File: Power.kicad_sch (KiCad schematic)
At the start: 53 parts, among them J16 19V 5A DC, Q2 AON7403, Q3 AON7403, Q4 AON7403, SW1 SW_Push, U11 LM3489QMM/NOPB, U6 LM3489QMM/NOPB, U8 LM3489QMM/NOPB

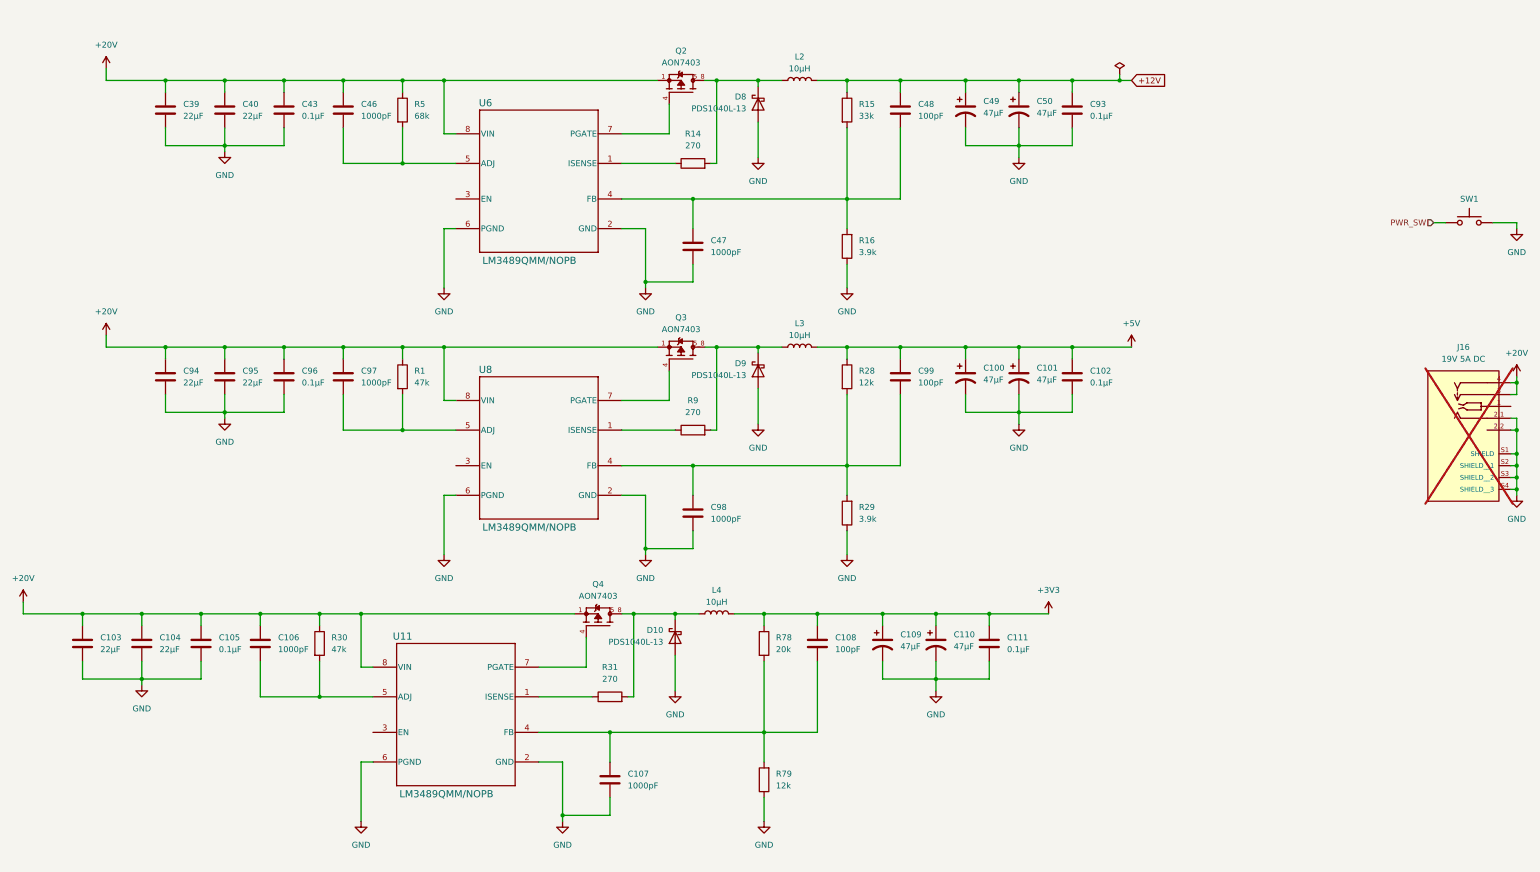
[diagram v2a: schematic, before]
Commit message: Rewired PCIe without redriver
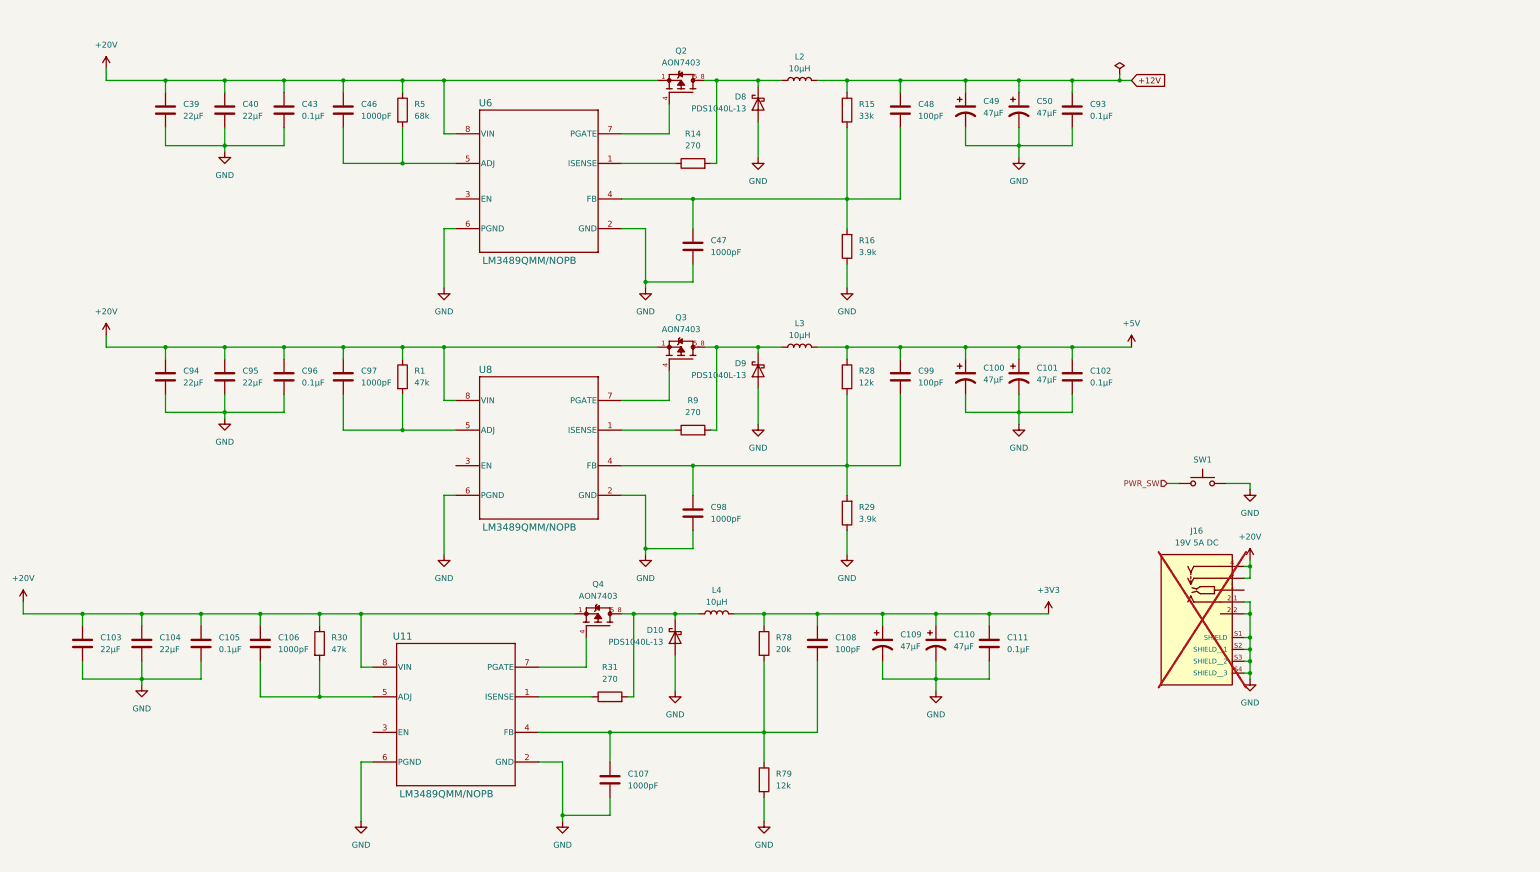
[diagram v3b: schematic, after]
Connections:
- net GND: now also R79.2; no longer R79.1
- net at C107.1, C108.2, R78.2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: now also R79.1; no longer R79.2
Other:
- moved on the sheet: J16, R79, SW1
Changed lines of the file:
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@@
 	)
 	(junction
-		(at 335.28 102.87)
+		(at 278.13 142.24)
 		(diameter 0)
 		(color 0 0 0 0)
 	)
 	(junction
-		(at 335.28 107.95)
+		(at 278.13 147.32)
 		(diameter 0)
 		(color 0 0 0 0)
@@
 	)
 	(junction
-		(at 335.28 115.57)
+		(at 278.13 154.94)
 		(diameter 0)
 		(color 0 0 0 0)
@@
 	)
 	(junction
-		(at 335.28 110.49)
+		(at 278.13 149.86)
 		(diameter 0)
 		(color 0 0 0 0)
@@
 	)
 	(junction
-		(at 335.28 113.03)
+		(at 278.13 152.4)
 		(diameter 0)
 		(color 0 0 0 0)
@@
 	)
 	(junction
-		(at 335.28 92.71)
+		(at 278.13 132.08)
 		(diameter 0)
 		(color 0 0 0 0)
@@
 	(wire
 		(pts
-			(xy 335.28 107.95) (xy 335.28 110.49)
+			(xy 278.13 147.32) (xy 278.13 149.86)
 		)
 		(stroke
@@
 	(wire
 		(pts
-			(xy 334.01 113.03) (xy 335.28 113.03)
+			(xy 276.86 152.4) (xy 278.13 152.4)
 		)
 		(stroke
@@
 	(wire
 		(pts
-			(xy 335.28 100.33) (xy 335.28 102.87)
+			(xy 278.13 139.7) (xy 278.13 142.24)
 		)
 		(stroke
@@
 	(wire
 		(pts
-			(xy 335.28 91.44) (xy 335.28 92.71)
+			(xy 278.13 130.81) (xy 278.13 132.08)
 		)
 		(stroke
@@
 	(wire
 		(pts
-			(xy 335.28 113.03) (xy 335.28 115.57)
+			(xy 278.13 152.4) (xy 278.13 154.94)
 		)
 		(stroke
@@
 	(wire
 		(pts
-			(xy 334.01 102.87) (xy 335.28 102.87)
+			(xy 276.86 142.24) (xy 278.13 142.24)
 		)
 		(stroke
@@
 	(wire
 		(pts
-			(xy 334.01 115.57) (xy 335.28 115.57)
+			(xy 276.86 154.94) (xy 278.13 154.94)
 		)
 		(stroke
@@
 	(wire
 		(pts
-			(xy 330.2 58.42) (xy 335.28 58.42)
+			(xy 273.05 114.3) (xy 278.13 114.3)
 		)
 		(stroke
@@
 	(wire
 		(pts
-			(xy 334.01 92.71) (xy 335.28 92.71)
+			(xy 276.86 132.08) (xy 278.13 132.08)
 		)
 		(stroke
@@
 	(wire
 		(pts
-			(xy 334.01 95.25) (xy 335.28 95.25)
+			(xy 276.86 134.62) (xy 278.13 134.62)
 		)
 		(stroke
@@
 	(wire
 		(pts
-			(xy 334.01 107.95) (xy 335.28 107.95)
+			(xy 276.86 147.32) (xy 278.13 147.32)
 		)
 		(stroke
@@
 	(wire
 		(pts
-			(xy 335.28 95.25) (xy 335.28 92.71)
+			(xy 278.13 134.62) (xy 278.13 132.08)
 		)
 		(stroke
@@
 	(wire
 		(pts
-			(xy 335.28 102.87) (xy 335.28 107.95)
+			(xy 278.13 142.24) (xy 278.13 147.32)
 		)
 		(stroke
@@
 	(wire
 		(pts
-			(xy 334.01 100.33) (xy 335.28 100.33)
+			(xy 276.86 139.7) (xy 278.13 139.7)
 		)
 		(stroke
@@
 	(wire
 		(pts
-			(xy 335.28 58.42) (xy 335.28 59.69)
+			(xy 278.13 114.3) (xy 278.13 115.57)
 		)
 		(stroke
@@
 	(wire
 		(pts
-			(xy 334.01 110.49) (xy 335.28 110.49)
+			(xy 276.86 149.86) (xy 278.13 149.86)
 		)
 		(stroke
@@
 	(wire
 		(pts
-			(xy 317.5 58.42) (xy 320.04 58.42)
+			(xy 260.35 114.3) (xy 262.89 114.3)
 		)
 		(stroke
@@
 	(wire
 		(pts
-			(xy 335.28 110.49) (xy 335.28 113.03)
+			(xy 278.13 149.86) (xy 278.13 152.4)
 		)
 		(stroke
@@
 	(wire
 		(pts
-			(xy 335.28 115.57) (xy 335.28 116.84)
+			(xy 278.13 154.94) (xy 278.13 156.21)
 		)
 		(stroke
@@
 	(hierarchical_label "PWR_SW"
 		(shape input)
-		(at 317.5 58.42 180)
+		(at 260.35 114.3 180)
 		(fields_autoplaced yes)
 		(effects
@@
 	(symbol
 		(lib_id "Switch:SW_Push")
-		(at 325.12 58.42 0)
+		(at 267.97 114.3 0)
 		(unit 1)
 		(exclude_from_sim no)
@@
 		(dnp no)
 		(property "Reference" "SW1"
-			(at 325.12 53.34 0)
+			(at 267.97 109.22 0)
 			(effects
 				(font
@@
 		)
 		(property "Value" "SW_Push"
-			(at 325.12 53.34 0)
+			(at 267.97 109.22 0)
 			(effects
 				(font
@@
 		)
 		(property "Footprint" "Button_Switch_SMD:SW_SPST_SKQG_WithStem"
-			(at 325.12 53.34 0)
+			(at 267.97 109.22 0)
 			(effects
 				(font
@@
 		)
 		(property "Datasheet" "~"
-			(at 325.12 53.34 0)
+			(at 267.97 109.22 0)
 			(effects
 				(font
@@
 		)
 		(property "Description" "Push button switch, generic, two pins"
-			(at 325.12 58.42 0)
+			(at 267.97 114.3 0)
 			(effects
 				(font
@@
 		)
 		(property "Part_Number" "TS-1187A-B-A-B"
-			(at 325.12 58.42 0)
+			(at 267.97 114.3 0)
 			(effects
 				(font
@@
 		)
 		(property "LCSC" "C318884"
-			(at 325.12 58.42 0)
+			(at 267.97 114.3 0)
 			(effects
 				(font
@@
 	(symbol
 		(lib_id "Device:R")
-		(at 173.99 177.8 180)
+		(at 173.99 177.8 0)
 		(unit 1)
 		(exclude_from_sim no)
@@
 					(size 1.27 1.27)
 				)
-				(justify right)
+				(justify left)
 			)
 		)
@@
 					(size 1.27 1.27)
 				)
-				(justify right)
+				(justify left)
 			)
 		)
 		(property "Footprint" "Resistor_SMD:R_0402_1005Metric"
-			(at 175.768 177.8 90)
+			(at 172.212 177.8 90)
 			(effects
 				(font
@@
 	(symbol
 		(lib_id "PJ-096H:PJ-096H")
-		(at 323.85 97.79 0)
+		(at 266.7 137.16 0)
 		(unit 1)
 		(exclude_from_sim no)
@@
 		(fields_autoplaced yes)
 		(property "Reference" "J16"
-			(at 323.85 85.09 0)
+			(at 266.7 124.46 0)
 			(effects
 				(font
@@
 		)
 		(property "Value" "19V 5A DC"
-			(at 323.85 87.63 0)
+			(at 266.7 127 0)
 			(effects
 				(font
@@
 		)
 		(property "Footprint" "PJ-096H:CUI_PJ-096H"
-			(at 323.85 97.79 0)
+			(at 266.7 137.16 0)
 			(effects
 				(font
@@
 		)
 		(property "Datasheet" "~"
-			(at 323.85 97.79 0)
+			(at 266.7 137.16 0)
 			(effects
 				(font
@@
 		)
 		(property "Description" "DC Barrel Jack"
-			(at 323.85 97.79 0)
+			(at 266.7 137.16 0)
 			(effects
 				(font
@@
 		)
 		(property "Part_Number" "PJ-096H"
-			(at 323.85 97.79 0)
+			(at 266.7 137.16 0)
 			(effects
 				(font
@@
 		)
 		(property "PARTREV" "1.0"
-			(at 323.85 97.79 0)
+			(at 266.7 137.16 0)
 			(effects
 				(font
@@
 		)
 		(property "STANDARD" "Manufacturer Recommendations"
-			(at 323.85 97.79 0)
+			(at 266.7 137.16 0)
 			(effects
 				(font
@@
 		)
 		(property "MANUFACTURER" "CUI"
-			(at 323.85 97.79 0)
+			(at 266.7 137.16 0)
 			(effects
 				(font
@@
 	(symbol
 		(lib_id "XG_Mobile:+20V")
-		(at 335.28 91.44 0)
+		(at 278.13 130.81 0)
 		(unit 1)
 		(exclude_from_sim no)
@@
 		(fields_autoplaced yes)
 		(property "Reference" "#PWR0105"
-			(at 335.28 95.25 0)
+			(at 278.13 134.62 0)
 			(effects
 				(font
@@
 		)
 		(property "Value" "+20V"
-			(at 335.28 86.36 0)
+			(at 278.13 125.73 0)
 			(effects
 				(font
@@
 		)
 		(property "Footprint" ""
-			(at 335.28 91.44 0)
+			(at 278.13 130.81 0)
 			(effects
 				(font
@@
 		)
 		(property "Datasheet" ""
-			(at 335.28 91.44 0)
+			(at 278.13 130.81 0)
 			(effects
 				(font
@@
 		)
 		(property "Description" "Power symbol creates a global label with name \"+20V\""
-			(at 335.28 91.44 0)
+			(at 278.13 130.81 0)
 			(effects
 				(font
@@
 	(symbol
 		(lib_id "power:GND")
-		(at 335.28 59.69 0)
+		(at 278.13 115.57 0)
 		(unit 1)
 		(exclude_from_sim no)
@@
 		(fields_autoplaced yes)
 		(property "Reference" "#PWR097"
-			(at 335.28 66.04 0)
+			(at 278.13 121.92 0)
 			(effects
 				(font
@@
 		)
 		(property "Value" "GND"
-			(at 335.28 64.77 0)
+			(at 278.13 120.65 0)
 			(effects
 				(font
@@
 		)
 		(property "Footprint" ""
-			(at 335.28 59.69 0)
+			(at 278.13 115.57 0)
 			(effects
 				(font
@@
 		)
 		(property "Datasheet" ""
-			(at 335.28 59.69 0)
+			(at 278.13 115.57 0)
 			(effects
 				(font
@@
 		)
 		(property "Description" "Power symbol creates a global label with name \"GND\" , ground"
-			(at 335.28 59.69 0)
+			(at 278.13 115.57 0)
 			(effects
 				(font
@@
 	(symbol
 		(lib_id "power:GND")
-		(at 335.28 116.84 0)
+		(at 278.13 156.21 0)
 		(mirror y)
 		(unit 1)
@@
 		(dnp no)
 		(property "Reference" "#PWR0104"
-			(at 335.28 123.19 0)
+			(at 278.13 162.56 0)
 			(effects
 				(font
@@
 		)
 		(property "Value" "GND"
-			(at 335.28 121.92 0)
+			(at 278.13 161.29 0)
 			(effects
 				(font
@@
 		)
 		(property "Footprint" ""
-			(at 335.28 116.84 0)
+			(at 278.13 156.21 0)
 			(effects
 				(font
@@
 		)
 		(property "Datasheet" ""
-			(at 335.28 116.84 0)
+			(at 278.13 156.21 0)
 			(effects
 				(font
@@
 		)
 		(property "Description" "Power symbol creates a global label with name \"GND\" , ground"
-			(at 335.28 116.84 0)
+			(at 278.13 156.21 0)
 			(effects
 				(font

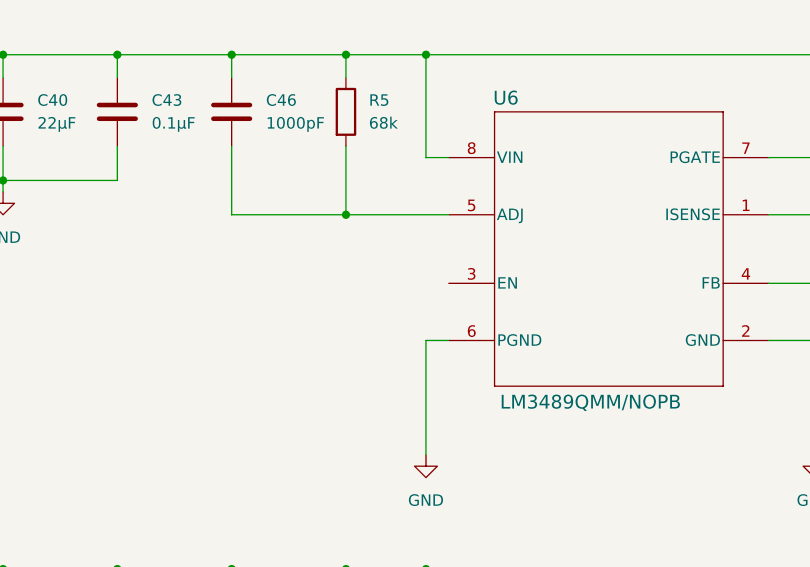
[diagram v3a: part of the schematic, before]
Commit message: Added MCU
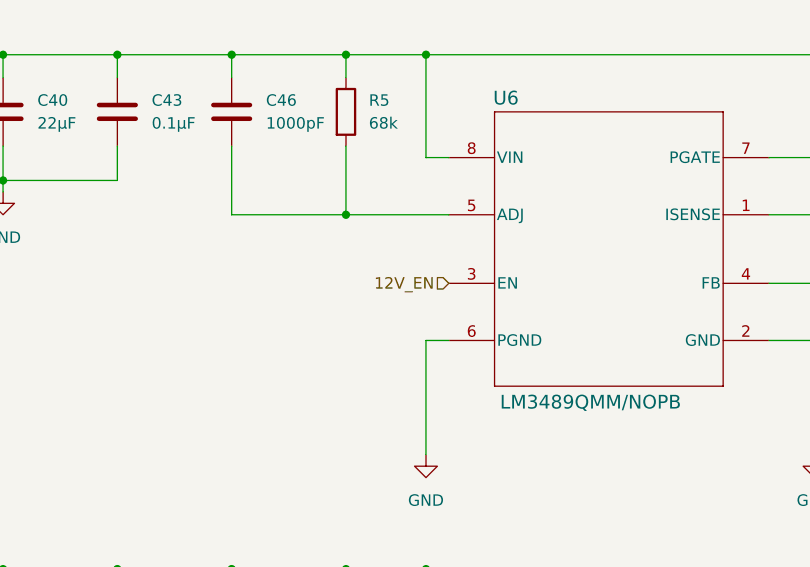
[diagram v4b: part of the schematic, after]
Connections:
- net 12V_EN: now reaches U6.3 (EN)
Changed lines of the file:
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@@
+		)
+	)
+	(hierarchical_label "12V_EN"
+		(shape input)
+		(at 107.95 53.34 180)
+		(fields_autoplaced yes)
+		(effects
+			(font
+				(size 1.27 1.27)
+			)
+			(justify right)
 		)
 	)

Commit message: Fixed all DRC errors
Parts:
- U11, U6, U8: footprint LM3489QMM-NOPB -> LM3489QMM-NOPB:LM3489QMM-NOPB
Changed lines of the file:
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@@
 			)
 		)
-		(property "Footprint" "LM3489QMM-NOPB"
+		(property "Footprint" "LM3489QMM-NOPB:LM3489QMM-NOPB"
 			(at 125.73 49.53 0)
 			(effects
@@
 			)
 		)
-		(property "Footprint" "LM3489QMM-NOPB"
+		(property "Footprint" "LM3489QMM-NOPB:LM3489QMM-NOPB"
 			(at 107.95 163.83 0)
 			(effects
@@
 			)
 		)
-		(property "Footprint" "LM3489QMM-NOPB"
+		(property "Footprint" "LM3489QMM-NOPB:LM3489QMM-NOPB"
 			(at 125.73 106.68 0)
 			(effects

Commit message: Replaced 12.4k resistor with two basic parts
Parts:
- L2, L3, L4: LCSC (none) -> C351119
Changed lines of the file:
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@@
 			)
 		)
+		(property "LCSC" "C351119"
+			(at 181.61 27.94 90)
+			(effects
+				(font
+					(size 1.27 1.27)
+				)
+				(hide yes)
+			)
+		)
 		(pin "2"
 		)
@@
 			)
 		)
+		(property "LCSC" "C351119"
+			(at 181.61 85.09 90)
+			(effects
+				(font
+					(size 1.27 1.27)
+				)
+				(hide yes)
+			)
+		)
 		(pin "2"
 		)
@@
 			(effects
 				(font
+					(size 1.27 1.27)
+				)
+				(hide yes)
+			)
+		)
+		(property "LCSC" "C351119"
+			(at 163.83 142.24 90)
+			(effects
+				(font

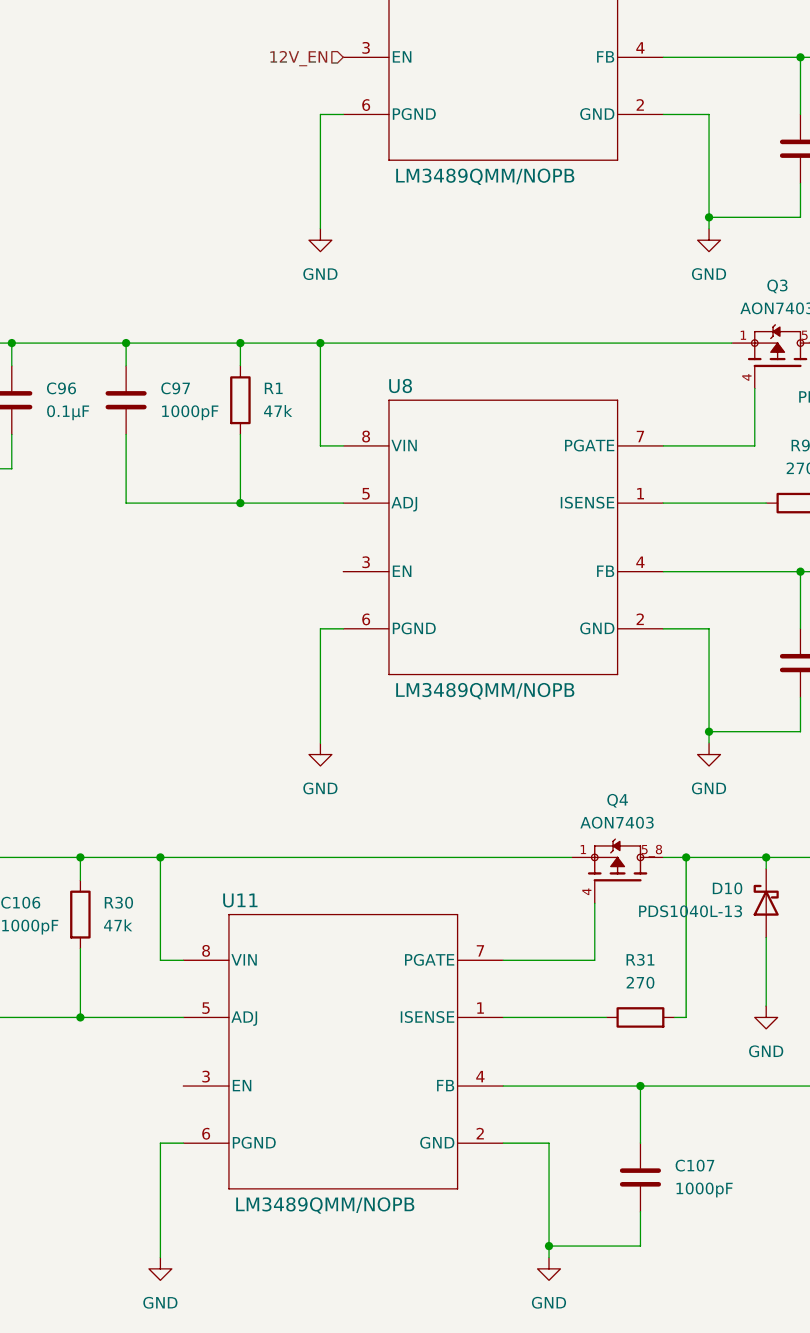
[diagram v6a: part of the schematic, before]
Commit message: Increased inductor size
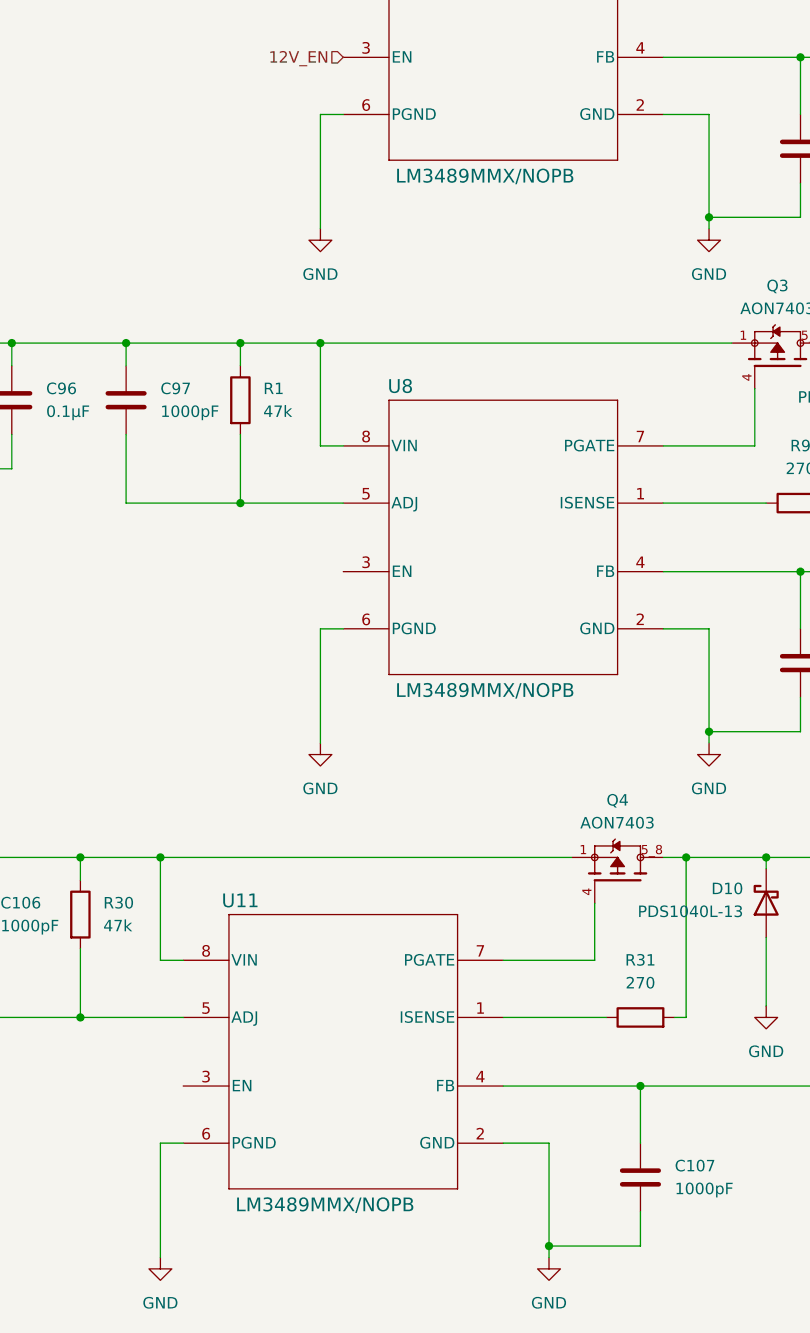
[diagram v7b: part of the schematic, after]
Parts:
- L2, L3, L4: LCSC C351119 -> C2880077; Part_Number YSPI0730-100M -> TMPA0605S-100MN-D
- U11, U6, U8: value LM3489QMM/NOPB -> LM3489MMX/NOPB; LCSC C2862414 -> C529297; Part_Number LM3489QMM/NOPB -> LM3489MMX/NOPB
